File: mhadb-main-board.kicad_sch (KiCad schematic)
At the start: 38 parts, among them J1 Conn_01x04_Pin, J2 USB_C_Receptacle_USB2.0_14P, SW1 SW_Push, SW2 SW_Push, U1 ESP32-S3FN8, U9 LDL212PV33R, Y1 48M

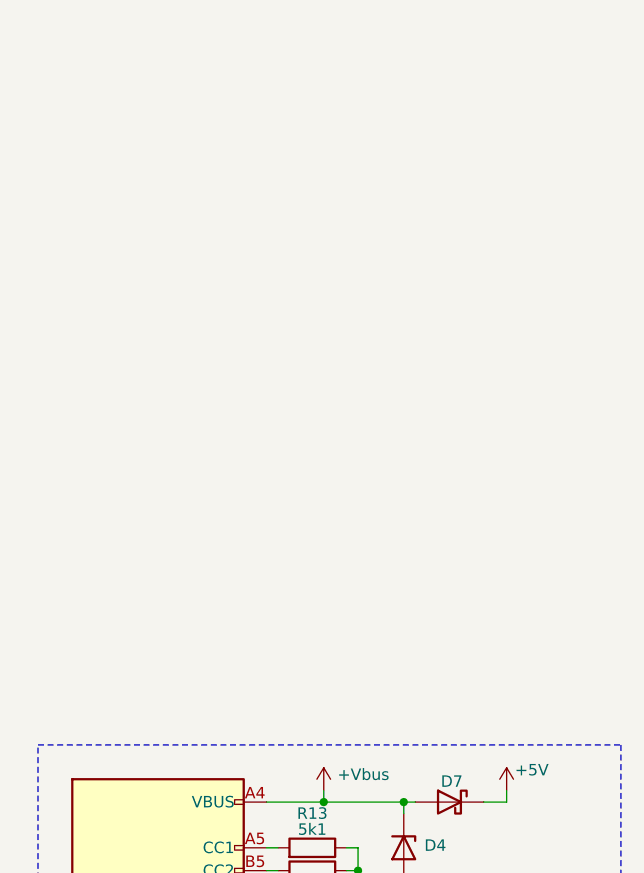
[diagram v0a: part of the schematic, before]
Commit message: schem: add 2 motor can/power connector
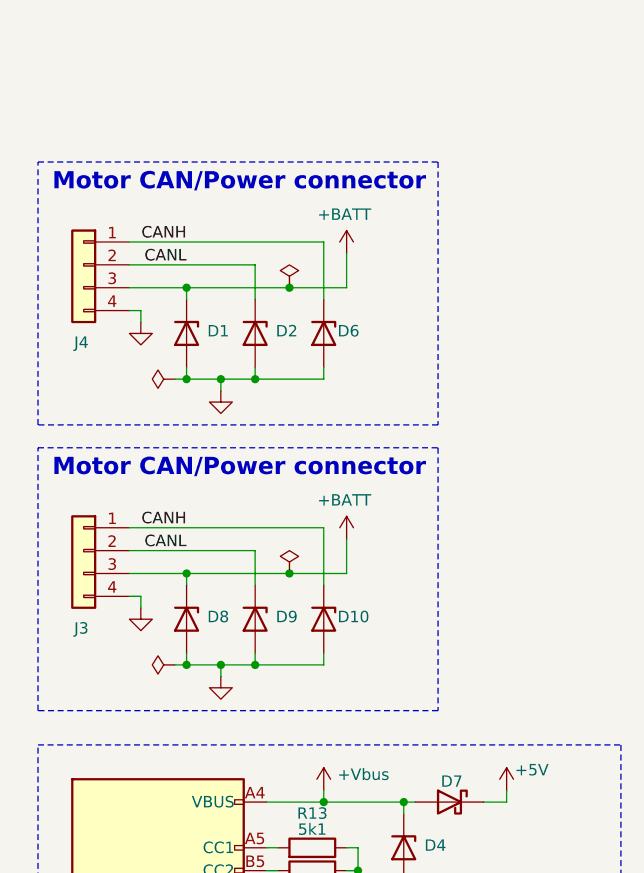
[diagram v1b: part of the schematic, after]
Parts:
- added D1, D10, D2, D6, D9: H5VU10U, GLCS:Diode_DFN1006, symbol GLCS:H5VU10U
- added J3, J4: Conn_01x04, Connector_JST:JST_XH_B4B-XH-A_1x04_P2.50mm_Vertical, symbol Connector_Generic:Conn_01x04
- renumbered D3 to D8
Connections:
- net GND: now also D1.2 (A), D10.2 (A), D2.2 (A), D6.2 (A), D9.2 (A), J3.4 (Pin_4), J4.4 (Pin_4)
- new net +BATT: D1.1 (K), D8.1 (K), J3.3 (Pin_3), J4.3 (Pin_3)
- new net CANH: D10.1 (K), D6.1 (K), J3.1 (Pin_1), J4.1 (Pin_1)
- new net CANL: D2.1 (K), D9.1 (K), J3.2 (Pin_2), J4.2 (Pin_2)
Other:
- note added: "Motor CAN/Power connector"

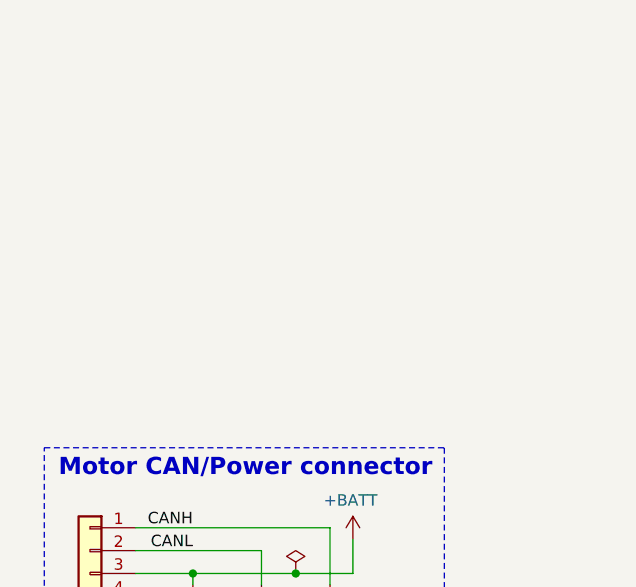
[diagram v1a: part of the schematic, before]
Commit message: schem: add line can/power connector
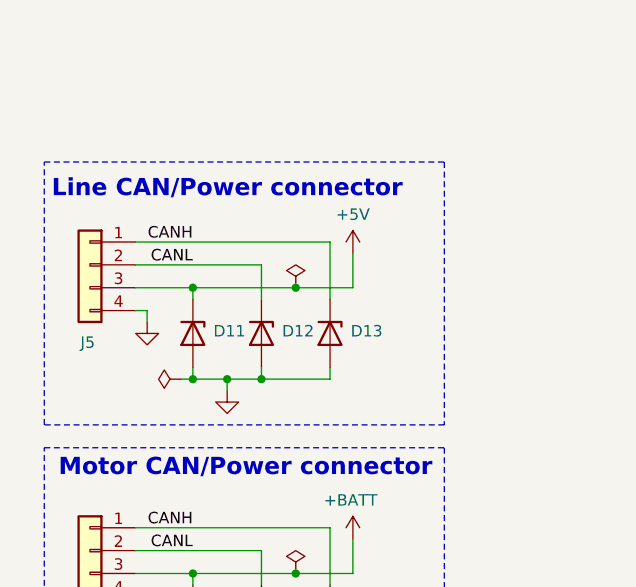
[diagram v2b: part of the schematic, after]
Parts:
- added D11, D12, D13: H5VU10U, GLCS:Diode_DFN1006, symbol GLCS:H5VU10U
- added J5: Conn_01x04, Connector_JST:JST_PH_S4B-PH-K_1x04_P2.00mm_Horizontal, symbol Connector_Generic:Conn_01x04
- renumbered D8 to D3
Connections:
- net +5V: now also D11.1 (K), J5.3 (Pin_3)
- net CANH: now also D13.1 (K), J5.1 (Pin_1)
- net CANL: now also D12.1 (K), J5.2 (Pin_2)
- net GND: now also D11.2 (A), D12.2 (A), D13.2 (A), J5.4 (Pin_4)
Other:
- note added: "Line CAN/Power connector"
- moved on the sheet: D8

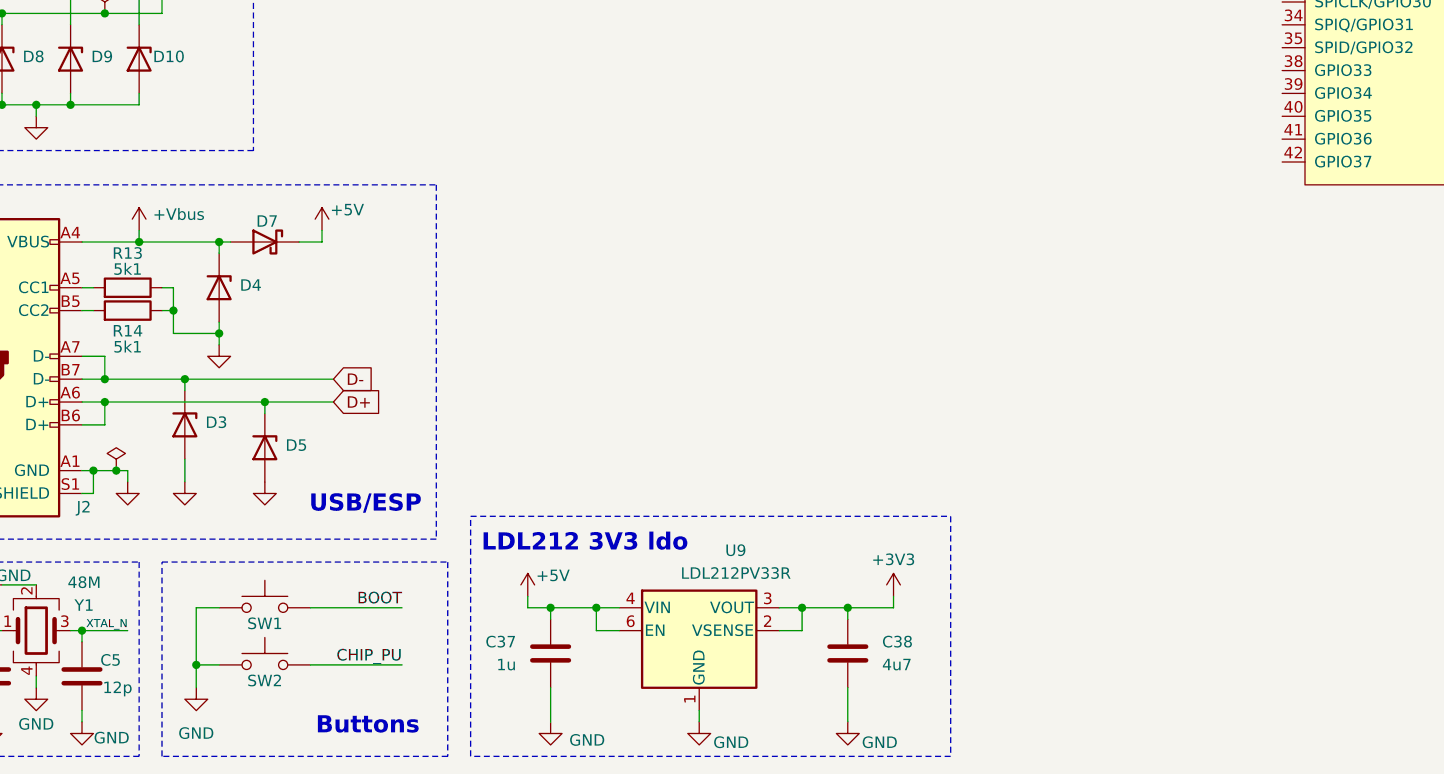
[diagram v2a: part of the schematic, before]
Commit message: schem: import TPS5430 5v from motor-power-poc
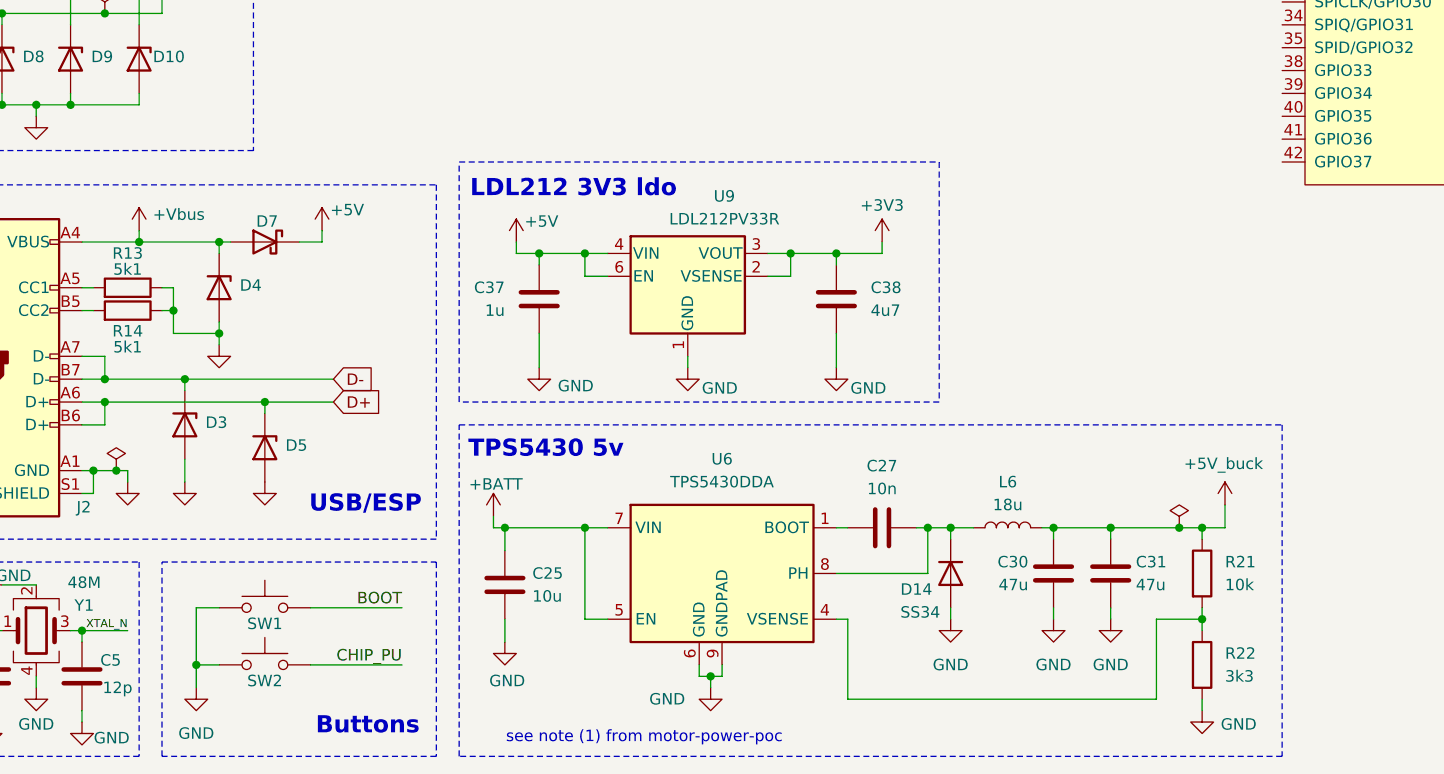
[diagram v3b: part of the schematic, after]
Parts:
- added C25: 10u, Capacitor_SMD:C_0805_2012Metric, symbol Device:C
- added C27: 10n, Capacitor_SMD:C_0402_1005Metric, symbol Device:C
- added C30, C31: 47u, Capacitor_SMD:C_1206_3216Metric, symbol Device:C
- added D14: SS34, Diode_SMD:D_SMA, symbol Device:D
- added L6: 18u, Inductor_SMD:L_Sunlord_SWRB1207S, symbol Device:L
- added R21: 10k, Resistor_SMD:R_0402_1005Metric, symbol Device:R
- added R22: 3k3, Resistor_SMD:R_0402_1005Metric, symbol Device:R
- added U6: TPS5430DDA, Package_SO:TI_SO-PowerPAD-8_ThermalVias, symbol Regulator_Switching:TPS5430DDA
- renumbered D3 to D8
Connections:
- net +BATT: now also C25.1, U6.5 (EN), U6.7 (VIN)
- net GND: now also C25.2, C30.2, C31.2, D14.2 (A), R22.2, U6.6 (GND), U6.9 (GNDPAD)
- new net: C27.2, D14.1 (K), L6.1, U6.8 (PH)
- new net: C27.1, U6.1 (BOOT)
- new net: R21.2, R22.1, U6.4 (VSENSE)
- new net +5V_buck: C30.1, C31.1, L6.2, R21.1
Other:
- note added: "TPS5430 5v"
- note added: "see note (1) from motor-power-poc"
- moved on the sheet: C37, C38, D3, U9

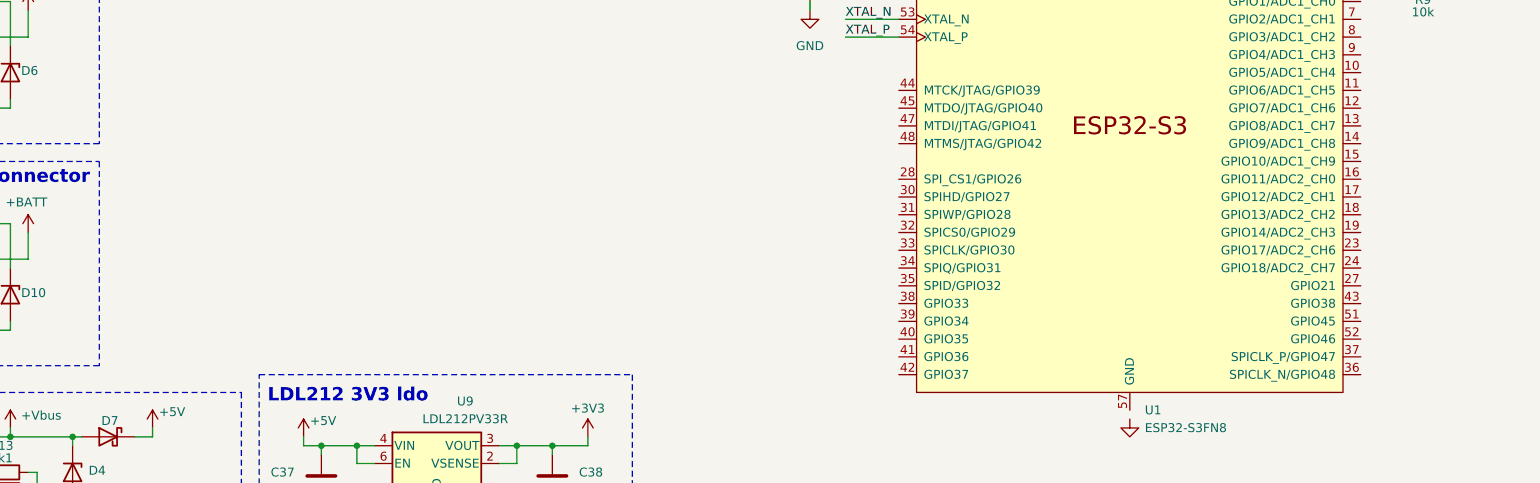
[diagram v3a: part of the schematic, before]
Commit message: schem: add SN65HVD230 CAN Transceiver
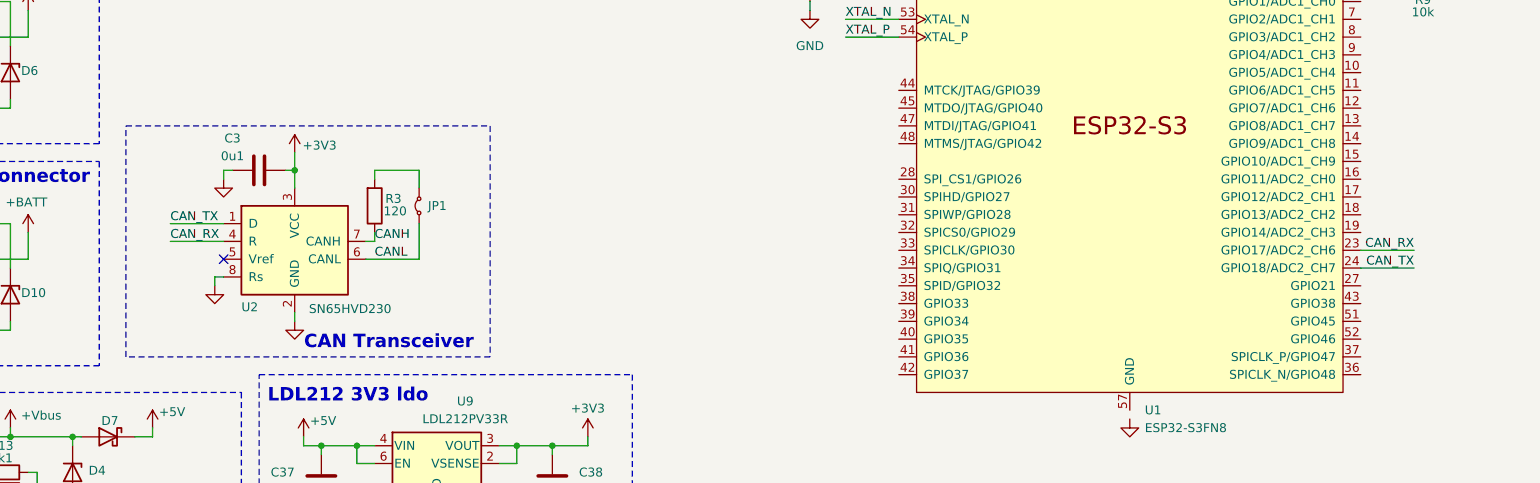
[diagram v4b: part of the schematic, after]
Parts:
- added C3: 0u1, Capacitor_SMD:C_0402_1005Metric, symbol Device:C
- added JP1: Jumper_2_Small_Bridged, Jumper:SolderJumper-2_P1.3mm_Open_RoundedPad1.0x1.5mm, symbol Jumper:Jumper_2_Small_Bridged
- added R3: 120, Resistor_SMD:R_1206_3216Metric, symbol Device:R
- added U2: SN65HVD230, Package_SO:SOIC-8_3.9x4.9mm_P1.27mm, symbol Interface_CAN_LIN:SN65HVD230
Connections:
- net +3V3: now also C3.1, U2.3 (VCC)
- net CANH: now also R3.1, U2.7 (CANH)
- net CANL: now also JP1.1 (A), U2.6 (CANL)
- net GND: now also C3.2, U2.2 (GND), U2.8 (Rs)
- net CAN_RX: now reaches U1.23 (GPIO17/ADC2_CH6)
- net CAN_RX: now also U2.4 (R)
- net CAN_TX: now reaches U1.24 (GPIO18/ADC2_CH7)
- net CAN_TX: now also U2.1 (D)
- new net: JP1.2 (B), R3.2
- no-connect marks 0 -> 1
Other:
- note added: "CAN Transceiver"

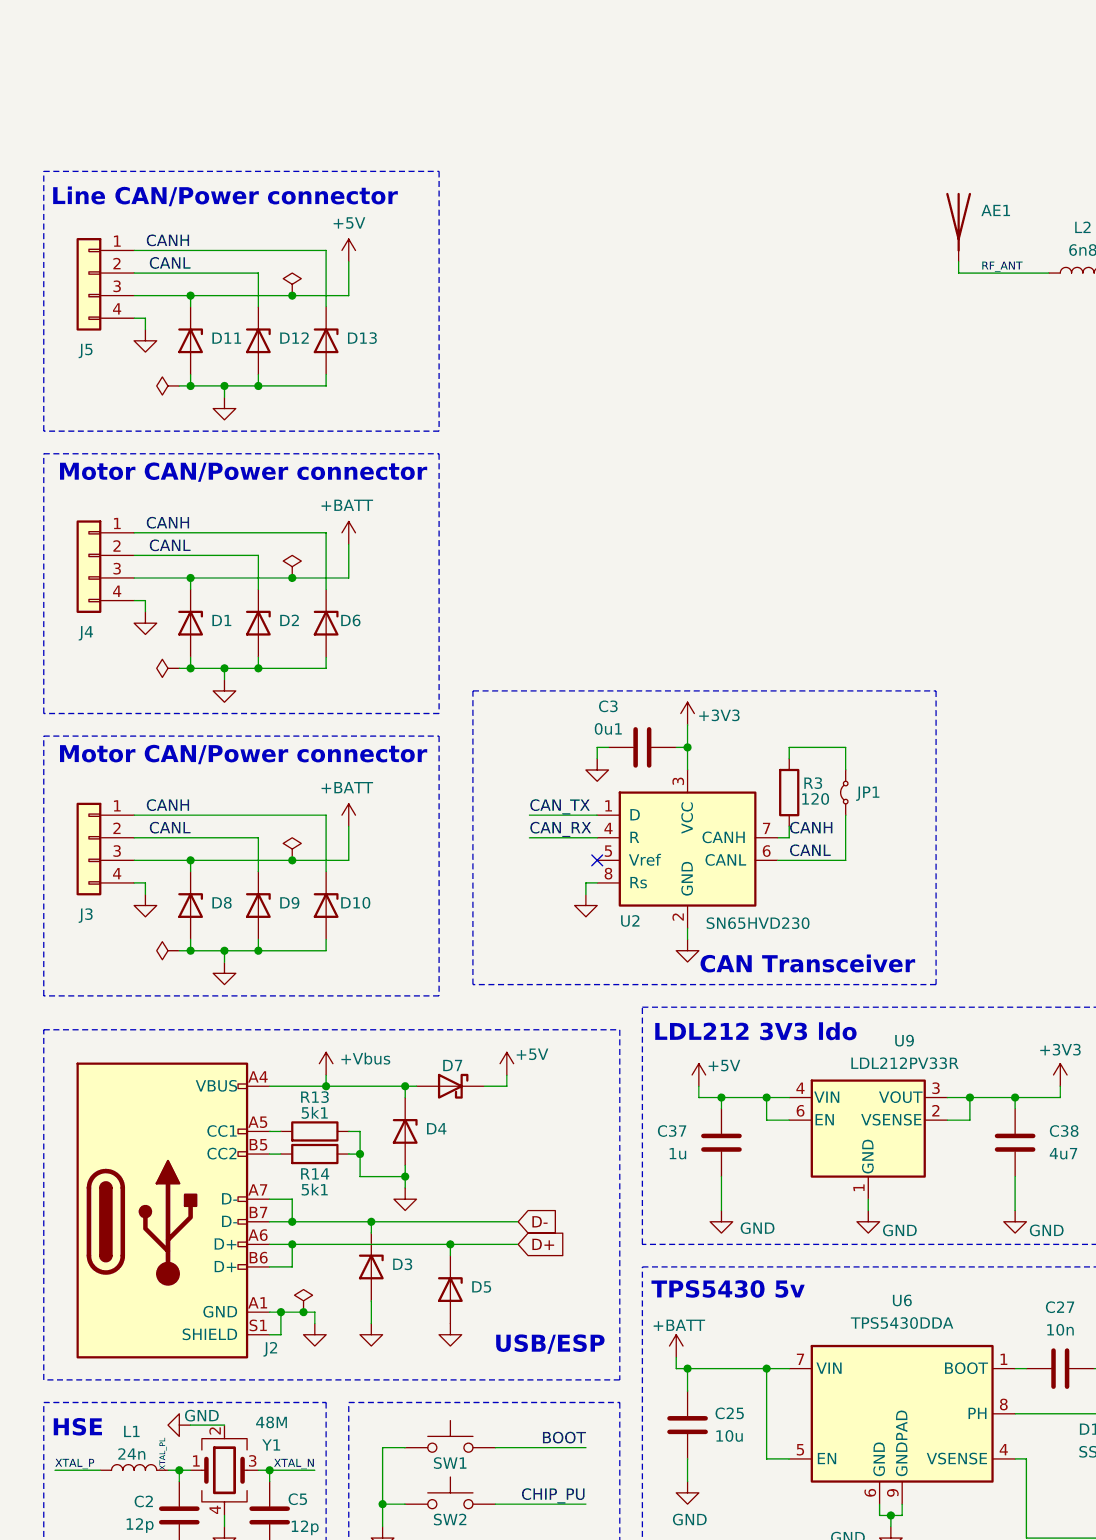
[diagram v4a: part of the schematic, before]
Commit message: schem: add XT30 battery connector
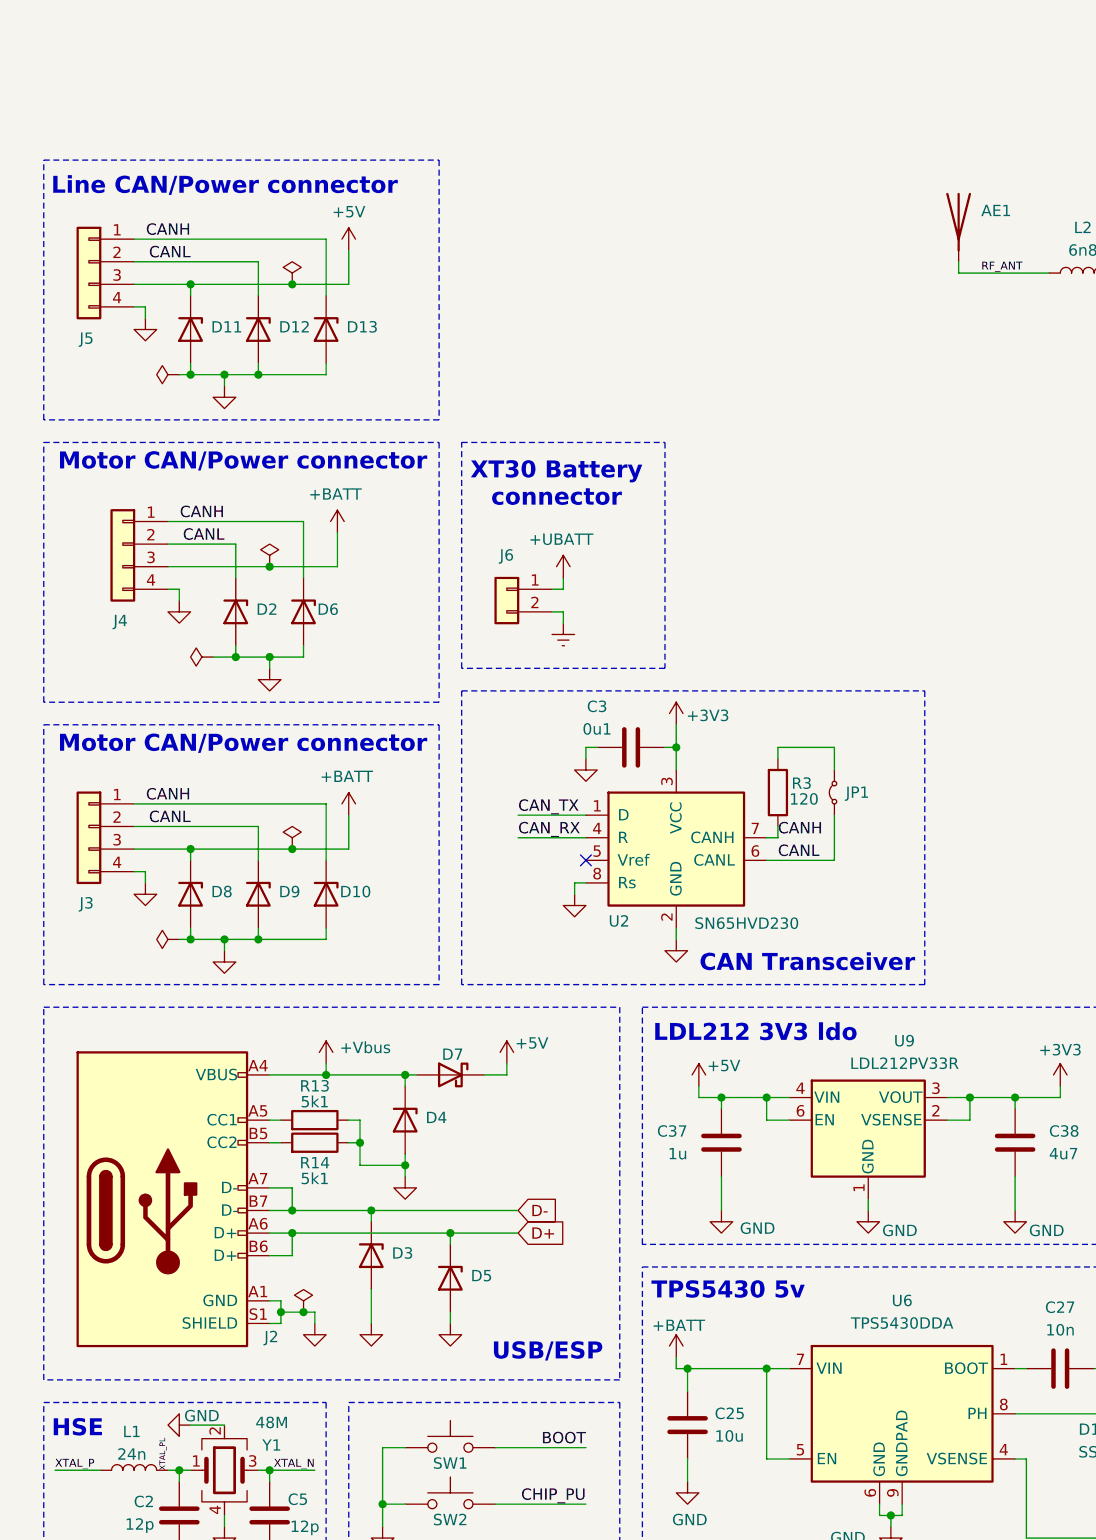
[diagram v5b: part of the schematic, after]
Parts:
- removed D1: H5VU10U, GLCS:Diode_DFN1006, symbol GLCS:H5VU10U
- added J6: Conn_01x02, Connector_AMASS:AMASS_XT30U-M_1x02_P5.0mm_Vertical, symbol Connector_Generic:Conn_01x02
- L4, L5: now left out of the parts list
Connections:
- new net +UBATT: J6.1 (Pin_1)
- new net BGND: J6.2 (Pin_2)
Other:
- note added: "XT30 Battery connector"
- moved on the sheet: C3, D10, D11, D12, D13, D2, D3, D4, D5, D6, D7, D9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
